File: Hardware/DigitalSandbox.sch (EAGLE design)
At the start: 80 parts, among them J1 AVR_SPI_PRG_6NS, Q1 MOSFET-N, Q2 MOSFET-P, U1 MCP73831, U2 ATMEGA328, U3 C2031N-1A2-B10K-GP, U4 MCP9700, U5 FT232RLSSOP, U6 LIGHTSENSORALS, U7 V_REG_LDOSMD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

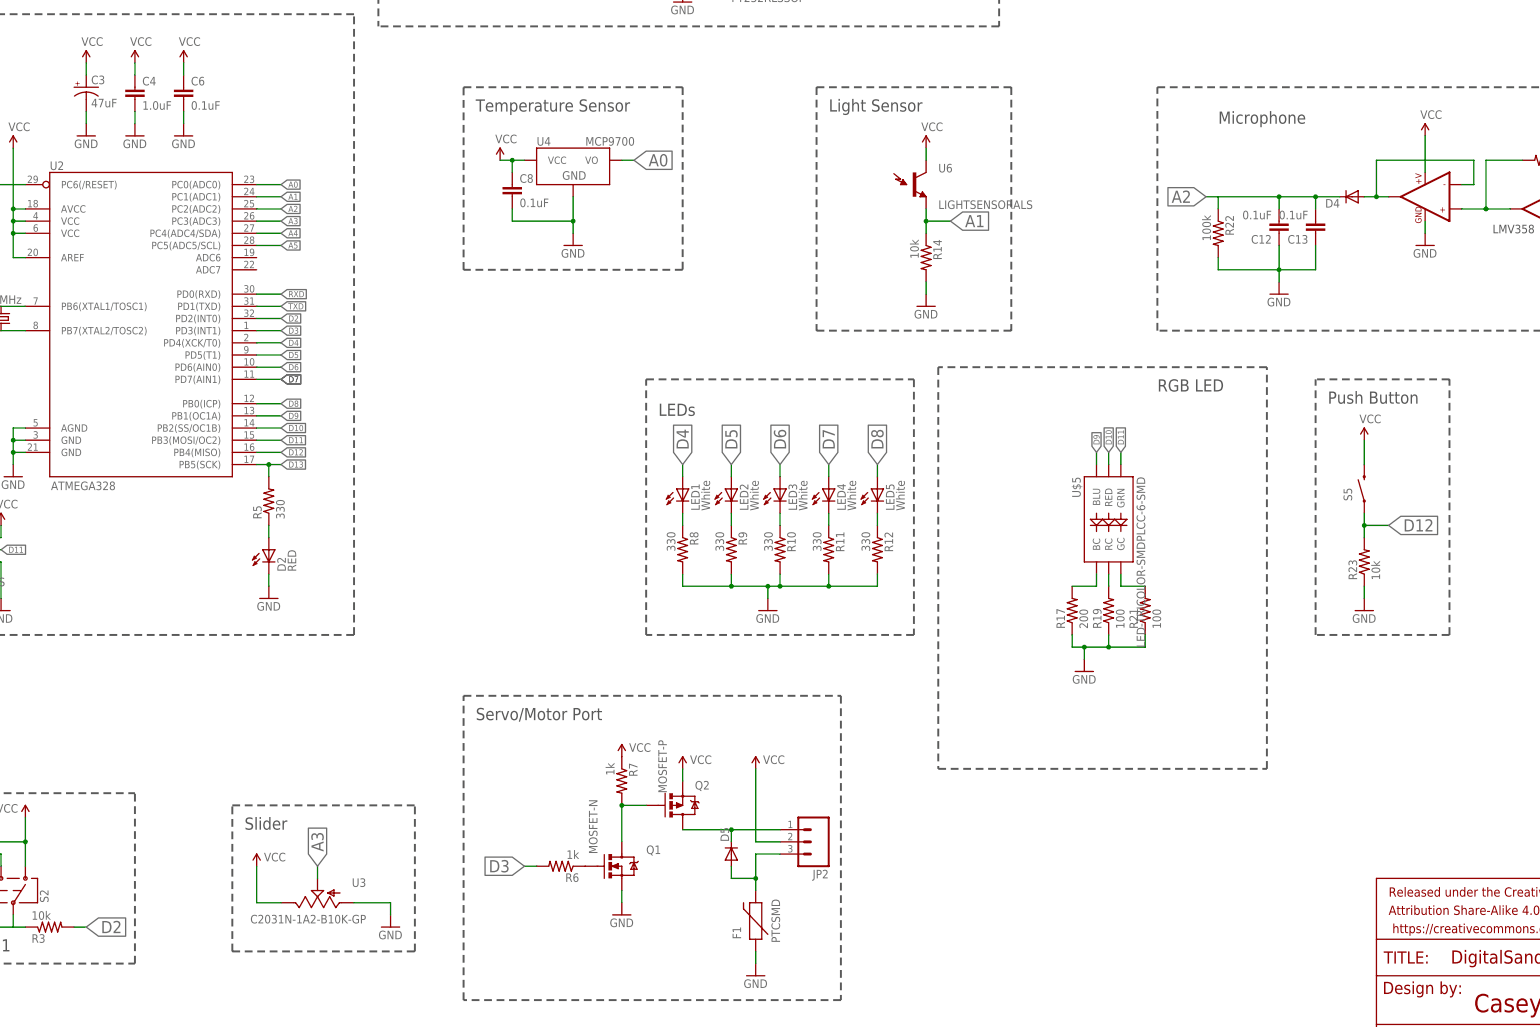
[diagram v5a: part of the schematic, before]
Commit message: reduced size of board by .15 inch in X
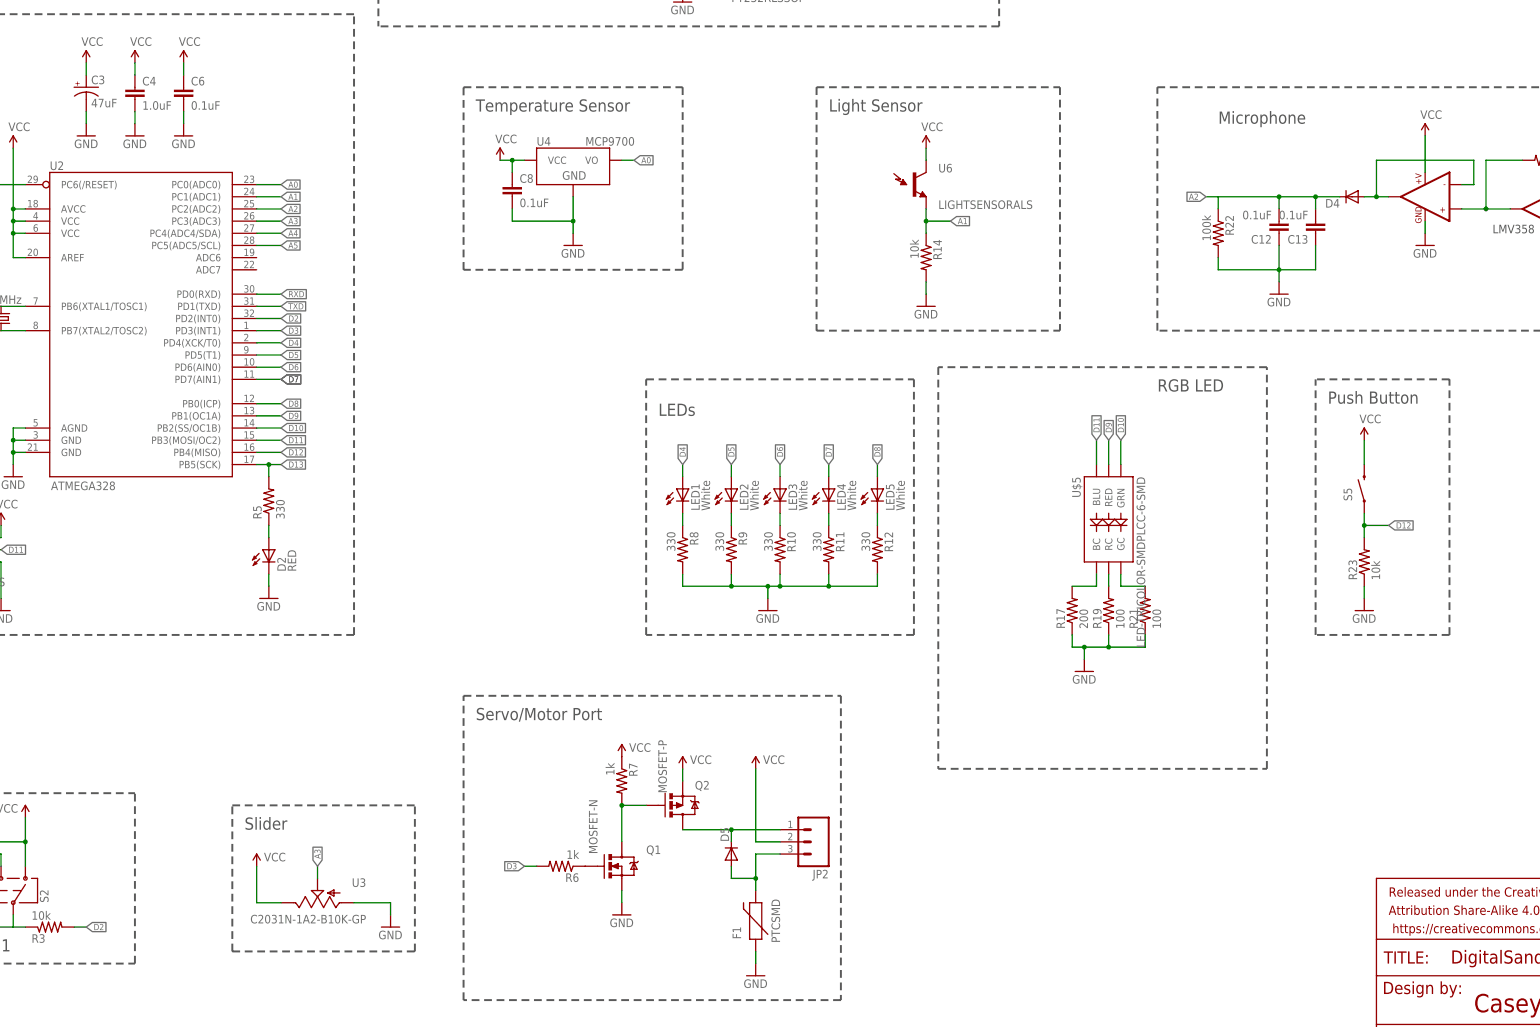
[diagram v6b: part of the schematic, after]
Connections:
- removed net N$28: R19.2, U$5.RC
- new net BLUE: R17.2, U$5.BC
- net D10: now also U$5.GRN; no longer U$5.RED
- net D11: now also U$5.BLU; no longer U$5.GRN
- net D9: now also U$5.RED; no longer U$5.BLU
- net RED: now also R19.2, U$5.RC; no longer R17.2, U$5.BC
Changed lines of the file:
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@@
 <wire x1="91.44" y1="20.32" x2="129.54" y2="20.32" width="0.4064" layer="97" style="shortdash"/>
 <wire x1="213.36" y1="200.66" x2="213.36" y2="149.86" width="0.4064" layer="97" style="shortdash"/>
-<wire x1="213.36" y1="149.86" x2="254" y2="149.86" width="0.4064" layer="97" style="shortdash"/>
-<wire x1="213.36" y1="200.66" x2="254" y2="200.66" width="0.4064" layer="97" style="shortdash"/>
-<wire x1="254" y1="200.66" x2="254" y2="149.86" width="0.4064" layer="97" style="shortdash"/>
+<wire x1="213.36" y1="149.86" x2="264.16" y2="149.86" width="0.4064" layer="97" style="shortdash"/>
+<wire x1="213.36" y1="200.66" x2="264.16" y2="200.66" width="0.4064" layer="97" style="shortdash"/>
+<wire x1="264.16" y1="200.66" x2="264.16" y2="149.86" width="0.4064" layer="97" style="shortdash"/>
 <wire x1="317.5" y1="86.36" x2="317.5" y2="139.7" width="0.4064" layer="97" style="shortdash"/>
 <wire x1="345.44" y1="139.7" x2="317.5" y2="139.7" width="0.4064" layer="97" style="shortdash"/>
@@
 </segment>
 <segment>
-<wire x1="276.86" y1="121.92" x2="276.86" y2="124.46" width="0.1524" layer="91"/>
-<label x="276.86" y="124.46" size="1.27" layer="95" rot="R90" xref="yes"/>
-<pinref part="U$5" gate="G$1" pin="GRN"/>
+<label x="271.78" y="127" size="1.27" layer="95" rot="R90" xref="yes"/>
+<wire x1="271.78" y1="121.92" x2="271.78" y2="127" width="0.1524" layer="91"/>
+<pinref part="U$5" gate="G$1" pin="BLU"/>
 </segment>
 <segment>
@@
 <segment>
 <wire x1="195.58" y1="119.38" x2="195.58" y2="121.92" width="0.1524" layer="91"/>
-<label x="195.58" y="121.92" size="2.54" layer="95" rot="R90" xref="yes"/>
+<label x="195.58" y="121.92" size="1.27" layer="95" rot="R90" xref="yes"/>
 <pinref part="LED2" gate="G$1" pin="A"/>
 </segment>
@@
 </segment>
 <segment>
-<label x="271.78" y="124.46" size="1.27" layer="95" rot="R90" xref="yes"/>
-<wire x1="271.78" y1="124.46" x2="271.78" y2="121.92" width="0.1524" layer="91"/>
-<pinref part="U$5" gate="G$1" pin="BLU"/>
+<label x="274.32" y="127" size="1.27" layer="95" rot="R90" xref="yes"/>
+<wire x1="274.32" y1="127" x2="274.32" y2="121.92" width="0.1524" layer="91"/>
+<pinref part="U$5" gate="G$1" pin="RED"/>
 </segment>
 </net>
@@
 <segment>
 <wire x1="205.74" y1="119.38" x2="205.74" y2="121.92" width="0.1524" layer="91"/>
-<label x="205.74" y="121.92" size="2.54" layer="95" rot="R90" xref="yes"/>
+<label x="205.74" y="121.92" size="1.27" layer="95" rot="R90" xref="yes"/>
 <pinref part="LED3" gate="G$1" pin="A"/>
 </segment>
@@
 </segment>
 <segment>
-<wire x1="274.32" y1="121.92" x2="274.32" y2="124.46" width="0.1524" layer="91"/>
-<label x="274.32" y="124.46" size="1.27" layer="95" rot="R90" xref="yes"/>
-<pinref part="U$5" gate="G$1" pin="RED"/>
+<label x="276.86" y="127" size="1.27" layer="95" rot="R90" xref="yes"/>
+<wire x1="276.86" y1="121.92" x2="276.86" y2="127" width="0.1524" layer="91"/>
+<pinref part="U$5" gate="G$1" pin="GRN"/>
 </segment>
 </net>
@@
 <pinref part="R22" gate="G$1" pin="1"/>
 <wire x1="297.18" y1="177.8" x2="294.64" y2="177.8" width="0.1524" layer="91"/>
-<label x="294.64" y="177.8" size="2.54" layer="95" rot="R180" xref="yes"/>
+<label x="294.64" y="177.8" size="1.27" layer="95" rot="R180" xref="yes"/>
 <pinref part="D4" gate="G$1" pin="C"/>
 </segment>
@@
 <wire x1="109.22" y1="38.1" x2="109.22" y2="35.56" width="0.1524" layer="91"/>
 <pinref part="U3" gate="G$1" pin="S"/>
-<label x="109.22" y="38.1" size="2.54" layer="95" rot="R90" xref="yes"/>
+<label x="109.22" y="38.1" size="1.27" layer="95" rot="R90" xref="yes"/>
 </segment>
 </net>
@@
 </segment>
 </net>
-<net name="RED" class="0">
+<net name="BLUE" class="0">
 <segment>
 <wire x1="266.7" y1="96.52" x2="271.78" y2="96.52" width="0.1524" layer="91"/>
@@
 <wire x1="175.26" y1="185.42" x2="172.72" y2="185.42" width="0.1524" layer="91"/>
 <pinref part="U4" gate="G$1" pin="VO"/>
-<label x="175.26" y="185.42" size="2.54" layer="95" xref="yes"/>
+<label x="175.26" y="185.42" size="1.27" layer="95" xref="yes"/>
 </segment>
 </net>
@@
 <pinref part="R3" gate="G$1" pin="2"/>
 <wire x1="58.42" y1="25.4" x2="60.96" y2="25.4" width="0.1524" layer="91"/>
-<label x="60.96" y="25.4" size="2.54" layer="95" rot="MR180" xref="yes"/>
+<label x="60.96" y="25.4" size="1.27" layer="95" rot="MR180" xref="yes"/>
 </segment>
 </net>
@@
 <pinref part="R6" gate="G$1" pin="2"/>
 <wire x1="154.94" y1="38.1" x2="152.4" y2="38.1" width="0.1524" layer="91"/>
-<label x="152.4" y="38.1" size="2.54" layer="95" rot="R180" xref="yes"/>
+<label x="152.4" y="38.1" size="1.27" layer="95" rot="R180" xref="yes"/>
 </segment>
 </net>
@@
 <segment>
 <wire x1="185.42" y1="119.38" x2="185.42" y2="121.92" width="0.1524" layer="91"/>
-<label x="185.42" y="121.92" size="2.54" layer="95" rot="R90" xref="yes"/>
+<label x="185.42" y="121.92" size="1.27" layer="95" rot="R90" xref="yes"/>
 <pinref part="LED1" gate="G$1" pin="A"/>
 </segment>
@@
 <segment>
 <wire x1="226.06" y1="119.38" x2="226.06" y2="121.92" width="0.1524" layer="91"/>
-<label x="226.06" y="121.92" size="2.54" layer="95" rot="R90" xref="yes"/>
+<label x="226.06" y="121.92" size="1.27" layer="95" rot="R90" xref="yes"/>
 <pinref part="LED5" gate="G$1" pin="A"/>
 </segment>
@@
 <segment>
 <wire x1="215.9" y1="119.38" x2="215.9" y2="121.92" width="0.1524" layer="91"/>
-<label x="215.9" y="121.92" size="2.54" layer="95" rot="R90" xref="yes"/>
+<label x="215.9" y="121.92" size="1.27" layer="95" rot="R90" xref="yes"/>
 <pinref part="LED4" gate="G$1" pin="A"/>
 </segment>
@@
 </segment>
 <segment>
-<label x="332.74" y="109.22" size="2.54" layer="95" xref="yes"/>
+<label x="332.74" y="109.22" size="1.27" layer="95" xref="yes"/>
 <pinref part="R23" gate="G$1" pin="2"/>
 <wire x1="332.74" y1="109.22" x2="327.66" y2="109.22" width="0.1524" layer="91"/>
@@
 <junction x="236.22" y="172.72"/>
 <pinref part="R14" gate="G$1" pin="1"/>
-<label x="241.3" y="172.72" size="2.54" layer="95" xref="yes"/>
+<label x="241.3" y="172.72" size="1.27" layer="95" xref="yes"/>
 <pinref part="U6" gate="G$1" pin="E1"/>
 </segment>
@@
 </segment>
 </net>
-<net name="N$28" class="0">
+<net name="RED" class="0">
 <segment>
 <pinref part="U$5" gate="G$1" pin="RC"/>

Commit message: Added Sparkle Values.
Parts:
- C1, C10, C11, C12, C13, C14, C6, C7, C8: device SparkFun:CAP0603-CAP -> SparkFun-Capacitors:0.1UF-25V(+80/-20%)(0603)
- C2, C5: device SparkFun-Passives:CAP0603-CAP -> SparkFun-Capacitors:4.7UF-6.3V-10%(0603)0603
- C3: device SparkFun:CAP_POL3528 -> SparkFun-Capacitors:47UF-10V-10%(TANT)
- C9: device SparkFun:CAP_POL1206 -> SparkFun-Capacitors:10UF-16V-10%(TANT)
- D1: device SparkFun:LED0603 -> SparkFun-LED:LED-YELLOW0603
- LED1, LED2, LED3, LED4, LED5: device SparkFun-LED:LED1206 -> SparkFun-LED:LED-WHITE
- LED6: device SparkFun:LED0603 -> SparkFun-LED:LED-RED0603
- LED7: device SparkFun:LED0603 -> SparkFun-LED:LED-GREEN0603
- Q2: device SparkFun-DiscreteSemi:MOSFET-PCHANNELSMD -> SparkFun-DiscreteSemi:MOSFET-PCHANNEL
- R1, R5: device SparkFun-Passives:RESISTOR0603-RES -> SparkFun-Resistors:330OHM1/10W1%(0603)
- R10, R11, R12, R8, R9: value 330 -> 300; device SparkFun-Resistors:33OHM1/10W1%(0603) -> SparkFun-Resistors:300OHM-1/10W-1%(0603)
- R13, R15, R6, R7: device SparkFun-Passives:RESISTOR0603-RES -> SparkFun-Resistors:1KOHM1/10W1%(0603)
- R14, R2, R23, R24, R26, R27, R3, R4: device SparkFun-Passives:RESISTOR0603-RES -> SparkFun-Resistors:10KOHM1/10W1%(0603)0603
- R17: value 200 -> 300; device SparkFun-Passives:RESISTOR0603-RES -> SparkFun-Resistors:300OHM-1/10W-1%(0603)
- R19, R21: device SparkFun-Passives:RESISTOR0603-RES -> SparkFun-Resistors:100OHM1/10W1%(0603)
- R22: device SparkFun-Passives:RESISTOR0603-RES -> SparkFun-Resistors:100KOHM1/10W1%(0603)
- R25: device SparkFun-Passives:RESISTOR0603-RES -> SparkFun-Resistors:2.2KOHM1/10W1%(0603)
- S1: device SparkFun:SWITCH-MOMENTARY-2SMD -> SparkFun-Electromechanical:TAC_SWITCHSMD
- S2: value AYZ0202 -> (none); device SparkFun:AYZ0202 -> SparkFun-Electromechanical:SWITCH-DPDTAYZ0202
- S3: device SparkFun:AYZ0202 -> SparkFun-Electromechanical:SWITCH-DPDTAYZ0202
- U1: device SparkFun:MCP73831 -> SparkFun-PowerIC:MCP73831
- U2: device SparkFun:ATMEGA168 -> SparkFun-DigitalIC:ATMEGA328_SMT
- U5: device SparkFun:FT232RLSSOP -> SparkFun-DigitalIC:FT232RLSSOP
- U8: value LMV358 -> LMV358SOIC; device SparkFun:LMV358 -> SparkFun-AnalogIC:LMV358SOIC
- U9: device SparkFun:MIC9.7MM -> SparkFun-Sensors:MIC9.7MM
- X1: value USB-SMD-NS -> USBSMD; device SparkFun:USB-SMD-NS -> SparkFun-Connectors:USBSMD
- Y1: device SparkFun:RESONATORSMD -> SparkFun-FreqCtrl:RESONATOR8MHZ
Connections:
- net 5V: now also S3.3, S3.6; no longer S3.1, S3.4
- net GND: now also S2.1, S2.4, U8G1.GND; no longer S2.3, S2.6, U8G$1.GND
- net N$20: now also U8G2.+IN2; no longer U8G$2.+IN2
- net N$23: now also U8G2.-IN2; no longer U8G$2.-IN2
- net N$24: now also U8G1.-IN1, U8G1.OUT1; no longer U8G$1.-IN1, U8G$1.OUT1
- net N$26: now also U8G1.+IN1, U8G2.OUT2; no longer U8G$1.+IN1, U8G$2.OUT2
- net VBATT: now also S3.1, S3.4; no longer S3.3, S3.6
- net VCC: now also S2.3, S2.6, U8G1.+V; no longer S2.1, S2.4, U8G$1.+V
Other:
- moved on the sheet: S3
